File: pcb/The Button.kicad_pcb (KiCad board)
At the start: 2 copper layers, 54 x 76 mm, 33 parts, among them J1 Conn_01x02, J2 2169890001, J4 Conn_01x02, J5 Conn_01x05_Pin, J6 Conn_01x03, J7 Conn_01x02, SW8 SW_SPST BOOT, U1 LD1117S33TR_SOT223, U2 STM32C071KBTx, U5 USBLC6-2SC6

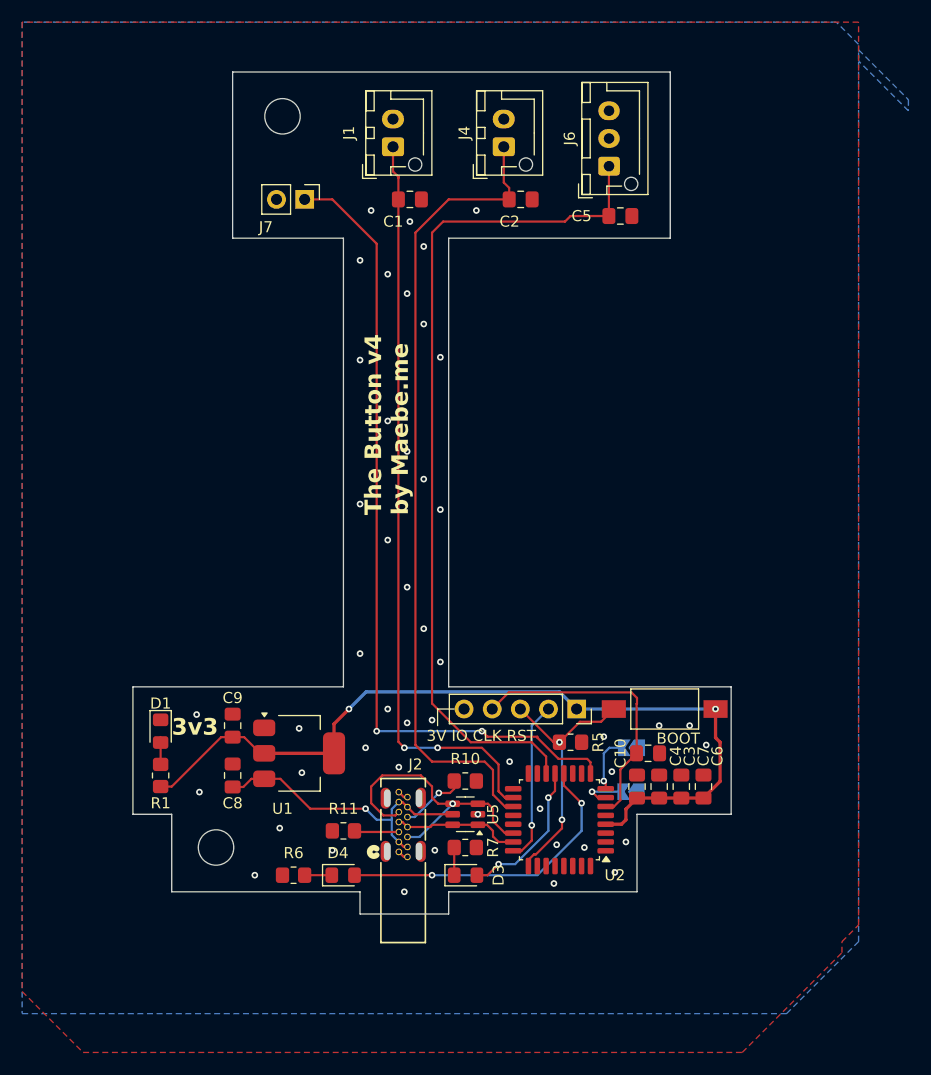
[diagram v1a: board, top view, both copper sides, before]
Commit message: Redesigned and rerouted
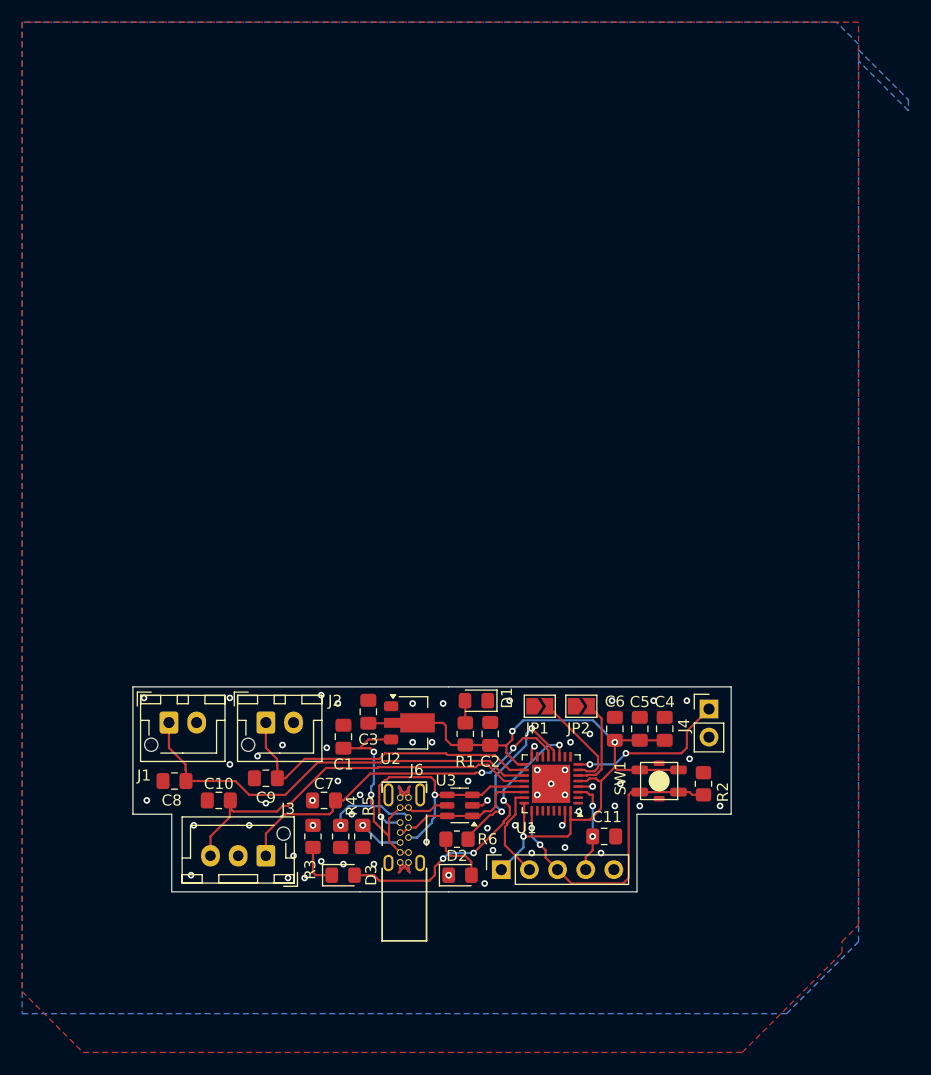
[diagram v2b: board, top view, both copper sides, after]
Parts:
- removed H1, H2: MountingHole, MountingHole:MountingHole_3.2mm_M3
- removed J7: Conn_01x02, Connector_PinHeader_2.54mm:PinHeader_1x02_P2.54mm_Vertical
- added C10: 100nF, Capacitor_SMD:C_0805_2012Metric_Pad1.18x1.45mm_HandSolder, F.Cu at (154.2, 89.8)
- added J4: Conn_01x02, Connector_PinHeader_2.54mm:PinHeader_1x02_P2.54mm_Vertical, F.Cu at (198.5, 81.5)
- C2: renamed from C4; value 100n -> 100nF
- C3: renamed from C9; value 10uF -> 22uF
- C4: renamed from C7; value 4.7Uf -> 4.7uF
- C6: renamed from C3; value 100n -> 100nF
- J6: renamed from J2; value 2169890001 -> USB-C-TH_MC-710S-Z13; footprint USB:216989-0001_MOL -> CustomUsb:USB_THT_SIDE_INSERT_14P
- JP1: renamed from JP2; moved to F.Cu
- JP2: renamed from JP1; moved to F.Cu
- SW1: renamed from SW8; footprint Button_Switch_SMD:SW_SPST_FSMSM -> Button_Switch_SMD:SW_PUSH_SPST_3X3MM
- U1: value LD1117S33TR_SOT223 -> STM32L071KBUx; footprint Package_TO_SOT_SMD:SOT-223-3_TabPin2 -> Package_DFN_QFN:QFN-32-1EP_5x5mm_P0.5mm_EP3.45x3.45mm
- U2: value STM32C071KBTx -> AMS1117-3.3; footprint Package_QFP:LQFP-32_7x7mm_P0.8mm -> Package_TO_SOT_SMD:SOT-89-3
- moved J3 69.5 mm to (158.5, 94.8), turned to 180 degrees
- moved C8 61.1 mm to (150.2, 88.0), turned to 180 degrees
- moved J1 60.1 mm to (149.8, 82.7), turned to 0 degrees
- moved C7 59.1 mm to (163.8, 89.8), turned to 180 degrees
- moved C9 53.8 mm to (158.5, 87.8), turned to 180 degrees
- moved J2 53.2 mm to (158.5, 82.7), turned to 0 degrees
- moved D1 28.6 mm to (177.5, 80.8), turned to 180 degrees
- moved R1 27.8 mm to (176.5, 83.8)
- moved U1 22.9 mm to (184.2, 88.2), turned to 180 degrees
- moved J5 16.0 mm to (179.8, 96.0), turned to 90 degrees
- moved U2 15.9 mm to (171.8, 82.8), turned to 0 degrees
- moved C2 14.1 mm to (178.8, 83.8)
- moved R2 12.6 mm to (198.0, 88.2), turned to 90 degrees
- moved C3 12.3 mm to (167.8, 81.8)
- moved R4 12.3 mm to (165.2, 93.0), turned to -90 degrees
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- renumbered C8 to C1, C10 to C11, C6 to C5, C5 to C7, C2 to C8, C1 to C9, D3 to D2, D4 to D3, J4 to J1, J1 to J2, J6 to J3, R5 to R2, R6 to R3, R10 to R4, R11 to R5, R7 to R6, U5 to U3
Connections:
- D2 pad 1: Net-(D3-K) (its old number) -> GND
- D2 pad 2: USR_LED_2 -> Net-(D2-A)
- J3 pad 3: unconnected-(J6-Pin_3-Pad3) -> BTN_KEY_NC
- R6 pad 1: Net-(D3-K) (its old number) -> USR_LED_2
- R6 pad 2: GND -> Net-(D2-A)
- U1 pad 1: GND -> unconnected-(U1-PC14-Pad1)
- U1 pad 2: VDD_3V -> unconnected-(U1-PC15-Pad2)
- U1 pad 3: VDDA_5V -> NRST
- U2 pad 1: unconnected-(U2-PB9-Pad1) -> GND
- U2 pad 2: unconnected-(U2-PC14-Pad2) -> VDD_3V
- U2 pad 3: unconnected-(U2-PC15-Pad3) -> VDDA_5V
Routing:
- net Net-(J7-Pin_1): track 73.7 -> 0.00 mm, vias 2 -> 0
- net BTN_KEY: track 77.4 -> 32.8 mm, vias 0 -> 2
- net BTN_HI: track 68.5 -> 29.3 mm, vias 2 -> 0
- net BTN_KEY_NC: track 0.00 -> 35.8 mm
- net BTN_LO: track 73.3 -> 38.7 mm
- net GND: track 1.93 -> 20.6 mm, vias 47 -> 60
- net NRST: track 25.3 -> 8.43 mm, vias 0 -> 2
- net Extra: track 0.00 -> 14.8 mm, vias 0 -> 2
- net VDD_3V: track 76.2 -> 64.5 mm, vias 2 -> 3
- net SWDIO: track 14.6 -> 8.59 mm, vias 1 -> 0
- net Net-(D2-A): track 0.00 -> 4.95 mm
- net HW_CFG_2: track 4.75 -> 9.40 mm, vias 1 -> 0
- net SWDCLK: track 23.6 -> 27.9 mm
- net HW_CFG_1: track 4.28 -> 8.50 mm, vias 1 -> 0
- net USR_LED_2: track 13.5 -> 16.7 mm
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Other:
- board size 54 x 76 mm -> 54 x 18.5 mm
- board text added: "TheButton.maebe.me Designed with Love, in Singapore"
- board text removed: "3V IO CLK RST"
- board text removed: "3v3"
- board text removed: "4mm"
- board text removed: "66mm"
- board text removed: "6mm"
- board text removed: "BOOT"
- board text removed: "The Button v4 by Maebe.me"

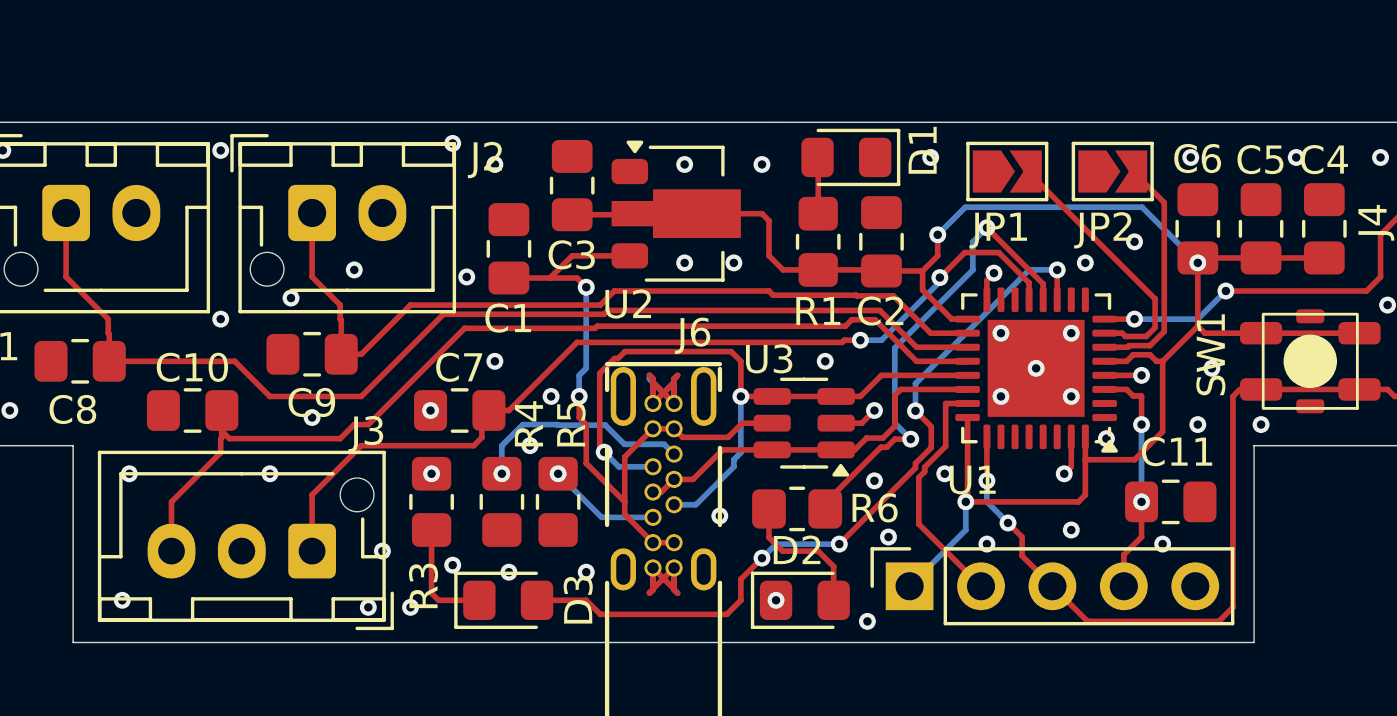
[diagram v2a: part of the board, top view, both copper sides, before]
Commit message: Fixed to use correct MCU - STM32*C*071, not L
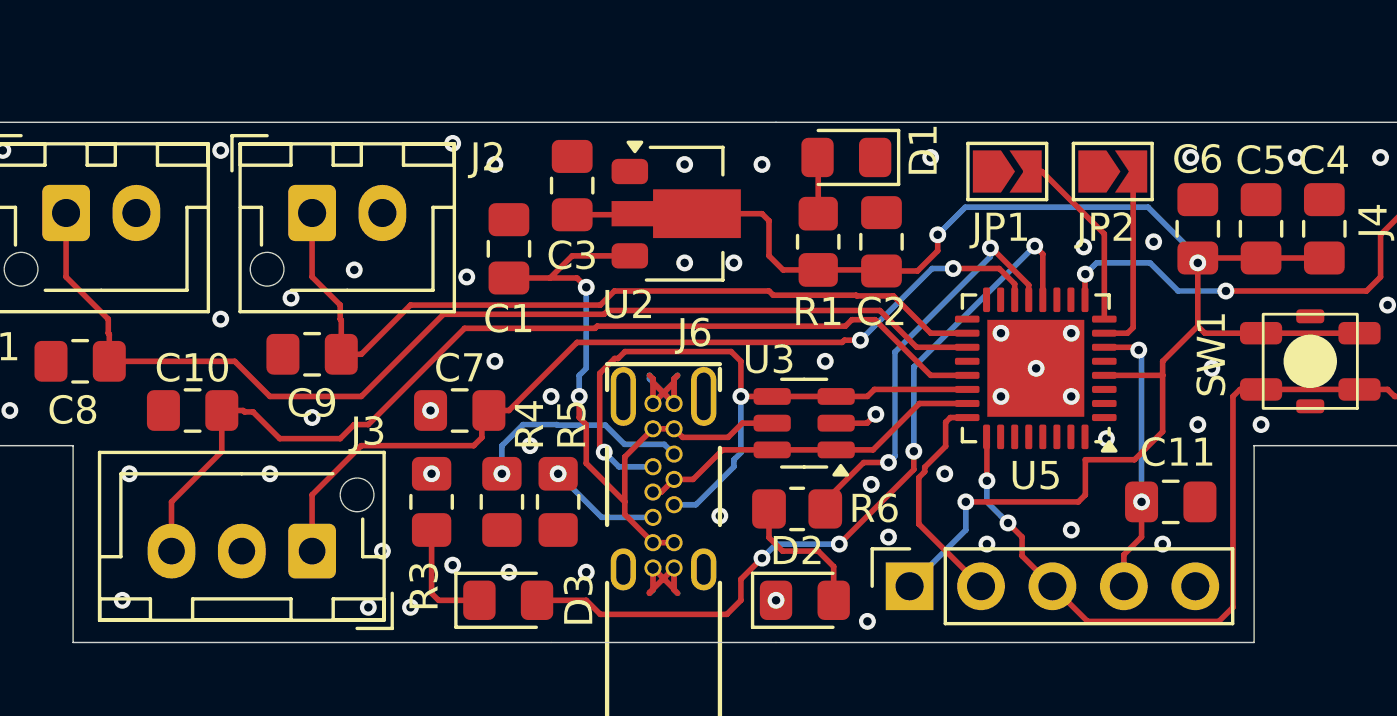
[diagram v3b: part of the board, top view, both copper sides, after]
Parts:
- removed U1: STM32L071KBUx, Package_DFN_QFN:QFN-32-1EP_5x5mm_P0.5mm_EP3.45x3.45mm
- added U5: STM32C071KBUx, Package_DFN_QFN:QFN-32-1EP_5x5mm_P0.5mm_EP3.45x3.45mm, F.Cu at (184.2, 88.2)
- C2: value 100nF -> 4.7uF
- C5: value 4.7uF -> 100nF
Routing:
- net VDD_3V: track 64.5 -> 57.9 mm
- net GND: track 20.6 -> 16.8 mm, vias 60 -> 57
- net HW_CFG_2: track 9.40 -> 6.67 mm
- net USR_LED_2: track 16.7 -> 14.7 mm
- net HW_CFG_1: track 8.50 -> 6.66 mm
- net Extra: track 14.8 -> 16.5 mm
- net NRST: track 8.43 -> 9.97 mm
- net BTN_KEY: track 32.8 -> 31.7 mm
- net D_P: track 13.3 -> 12.5 mm
- net SWDIO: track 8.59 -> 7.98 mm
- net BTN_KEY_NC: track 35.8 -> 35.2 mm
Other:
- board text added: "TheButton.maebe.me Designed with love, in Singapore"
- board text removed: "TheButton.maebe.me Designed with Love, in Singapore"
